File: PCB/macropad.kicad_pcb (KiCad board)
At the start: 2 copper layers, 80.5 x 100 mm, 46 parts, among them SW1 Kailh Choc V2, SW10 Kailh Choc V2, SW11 Kailh Choc V2, SW12 Kailh Choc V2, SW13 Kailh Choc V2, SW14 Kailh Choc V2, SW15 Kailh Choc V2, SW16 Kailh Choc V2, SW2 Kailh Choc V2, SW3 Kailh Choc V2, SW4 Kailh Choc V2, SW5 Kailh Choc V2, SW6 Kailh Choc V2, SW7 Kailh Choc V2, SW8 Kailh Choc V2, SW9 Kailh Choc V2, U2 SEEEDUINO XIAO RP2040

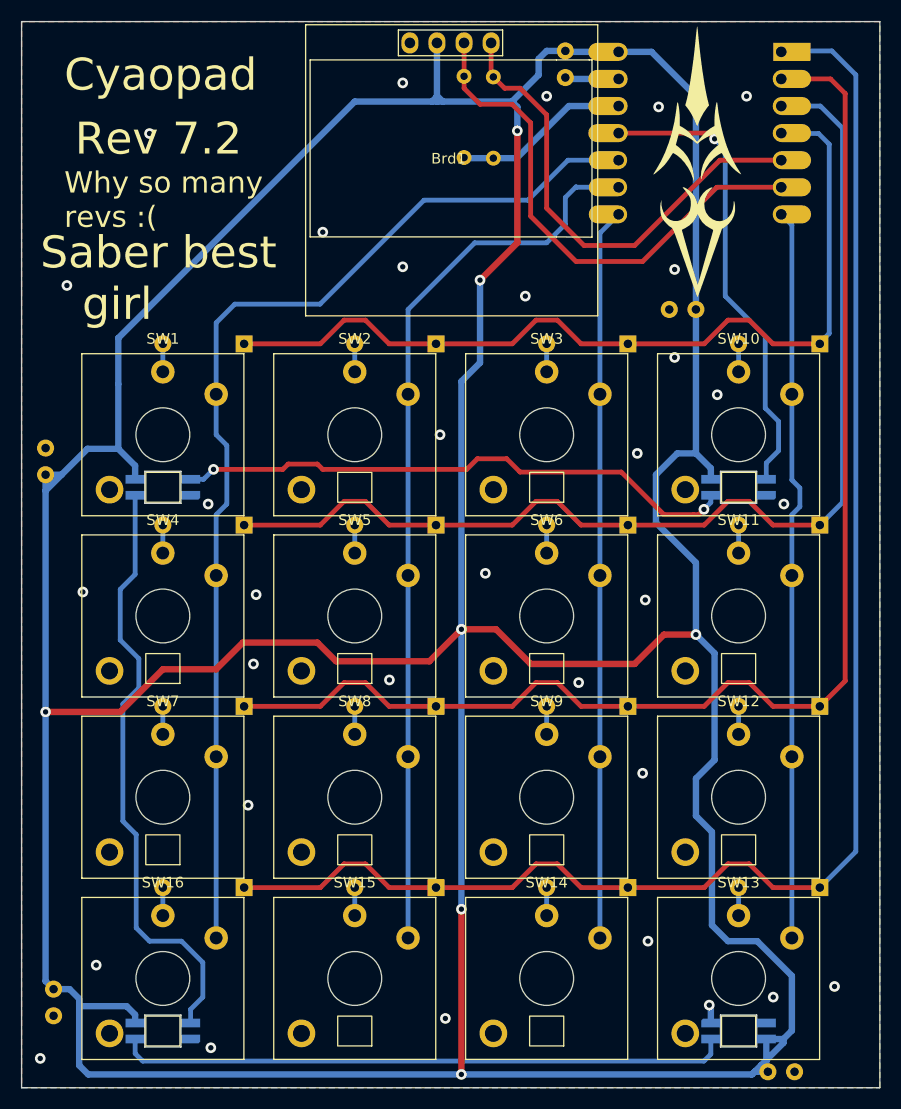
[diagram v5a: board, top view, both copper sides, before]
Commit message: Firmware path + clean up tracks
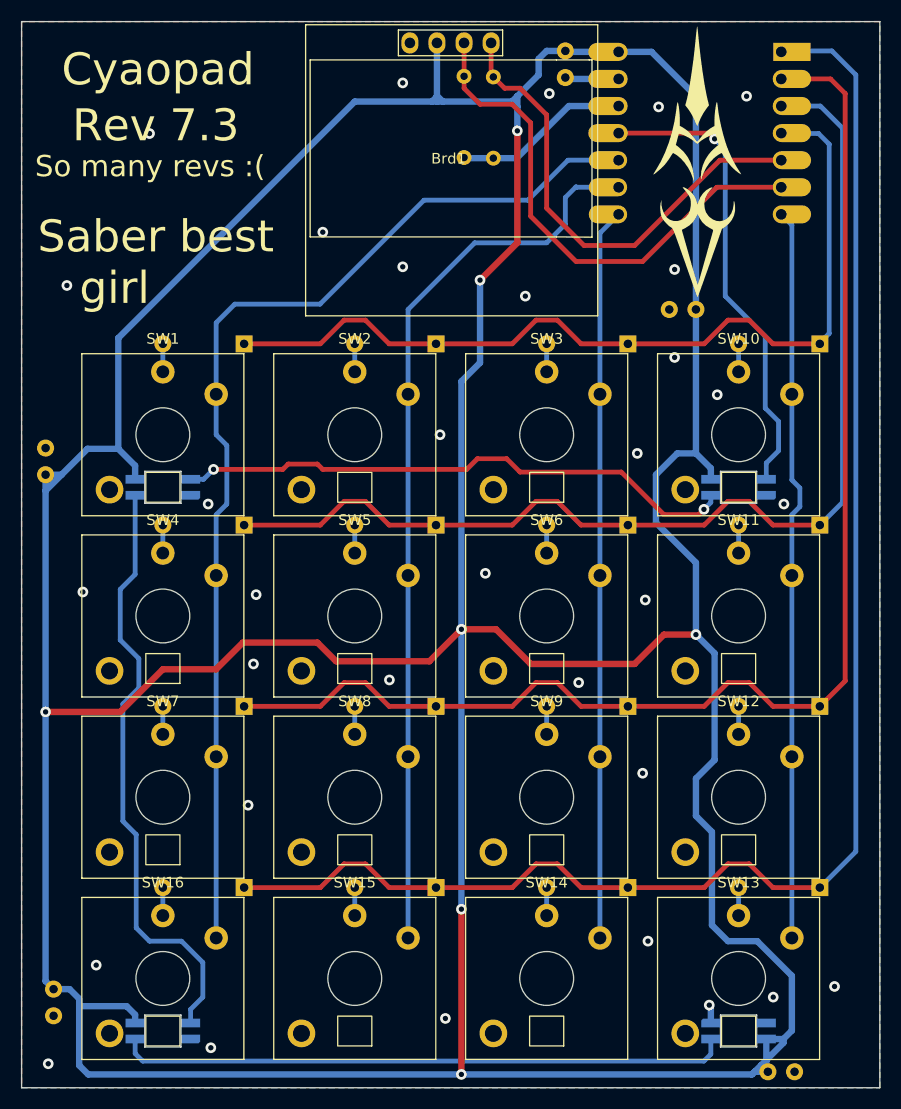
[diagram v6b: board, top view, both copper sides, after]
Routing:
- net +5V: track 502.4 -> 503.4 mm
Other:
- board text added: "Rev 7.3"
- board text added: "So many revs :("
- board text removed: "Rev 7.2"
- board text removed: "Why so many revs :("
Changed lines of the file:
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@@
     (title "Cyao macropad")
     (date "2024-09-23")
-    (rev "v7.2")
+    (rev "v7.3")
     (company "Cheyao")
     (comment 1 "https://github.com/cheyao/macropad")
@@
   (gr_line (start 185 150) (end 185 50)
     (stroke (width 0.05) (type default)) (layer "Edge.Cuts"))
-  (gr_text "Saber best\n   girl" (at 106.25 78.25) (layer "F.SilkS")
+  (gr_text "Saber best\n   girl" (at 106 76.75) (layer "F.SilkS")
     (effects (font (size 3 3) (thickness 0.3)) (justify left bottom))
   )
-  (gr_text "Rev 7.2" (at 109.5 62.75) (layer "F.SilkS")
+  (gr_text "Rev 7.3" (at 109.25 61.5) (layer "F.SilkS")
     (effects (font (size 3 3) (thickness 0.3)) (justify left bottom))
   )
-  (gr_text "Cyaopad" (at 108.5 56.75) (layer "F.SilkS")
+  (gr_text "Cyaopad" (at 108.25 56.25) (layer "F.SilkS")
     (effects (font (size 3 3) (thickness 0.3)) (justify left bottom))
   )
-  (gr_text "Why so many \nrevs :(" (at 108.5 69.5) (layer "F.SilkS")
+  (gr_text "So many revs :(" (at 105.75 64.75) (layer "F.SilkS")
     (effects (font (size 2 2) (thickness 0.3)) (justify left bottom))
   )
@@
   (via (at 165.75 73.25) (size 1) (drill 0.5) (layers "F.Cu" "B.Cu") (free) (net 26))
   (via (at 143.75 88.75) (size 1) (drill 0.5) (layers "F.Cu" "B.Cu") (free) (net 26))
-  (via (at 153.75 57) (size 1) (drill 0.5) (layers "F.Cu" "B.Cu") (free) (net 26))
+  (via (at 154 56.75) (size 1) (drill 0.5) (layers "F.Cu" "B.Cu") (free) (net 26))
   (via (at 148 101.75) (size 1) (drill 0.5) (layers "F.Cu" "B.Cu") (free) (net 26))
   (via (at 151.75 75.75) (size 1) (drill 0.5) (layers "F.Cu" "B.Cu") (free) (net 26))
-  (via (at 106.25 147.25) (size 1) (drill 0.5) (layers "F.Cu" "B.Cu") (free) (net 26))
+  (via (at 107 147.75) (size 1) (drill 0.5) (layers "F.Cu" "B.Cu") (free) (net 26))
   (via (at 126.25 110.25) (size 1) (drill 0.5) (layers "F.Cu" "B.Cu") (free) (net 26))
   (via (at 163 104.25) (size 1) (drill 0.5) (layers "F.Cu" "B.Cu") (free) (net 26))
@@
   (segment (start 143.46 52) (end 143.46 56.96) (width 0.6) (layer "B.Cu") (net 27))
   (segment (start 106.75 92.5) (end 108.25 92.5) (width 0.6) (layer "B.Cu") (net 27))
-  (segment (start 113.57 84) (end 113.57 90.07) (width 0.6) (layer "B.Cu") (net 27))
+  (segment (start 113.57 79.68) (end 113.57 90.07) (width 0.6) (layer "B.Cu") (net 27))
   (segment (start 173.875 147.875) (end 174.35 147.4) (width 0.6) (layer "B.Cu") (net 27))
   (segment (start 176.75 139.5) (end 176.75 144.64) (width 0.6) (layer "B.Cu") (net 27))
+  (segment (start 151 58) (end 151 57) (width 0.6) (layer "B.Cu") (net 27))
   (segment (start 113.57 79.68) (end 135.75 57.5) (width 0.6) (layer "B.Cu") (net 27))
   (segment (start 166 90.5) (end 164 92.5) (width 0.6) (layer "B.Cu") (net 27))
@@
   (segment (start 174.35 148.35) (end 174.5 148.5) (width 0.6) (layer "B.Cu") (net 27))
   (segment (start 175.96 145.43) (end 175.96 145.79) (width 0.6) (layer "B.Cu") (net 27))
+  (segment (start 151 57) (end 153 55) (width 0.6) (layer "B.Cu") (net 27))
   (segment (start 169.25 126) (end 169.25 134.75) (width 0.6) (layer "B.Cu") (net 27))
   (segment (start 110.75 148.75) (end 173 148.75) (width 0.6) (layer "B.Cu") (net 27))
@@
   (segment (start 114.35 142.35) (end 115.15 143.15) (width 0.6) (layer "B.Cu") (net 27))
   (segment (start 143.46 57.04) (end 143.5 57.08) (width 0.6) (layer "B.Cu") (net 27))
-  (segment (start 113.57 84) (end 113.57 79.68) (width 0.6) (layer "B.Cu") (net 27))
   (segment (start 144 57.5) (end 143.5 57.5) (width 0.6) (layer "B.Cu") (net 27))
+  (segment (start 150.5 57.5) (end 151 57) (width 0.6) (layer "B.Cu") (net 27))
   (segment (start 160.5 52.84) (end 155.59 52.84) (width 0.6) (layer "B.Cu") (net 27))
-  (segment (start 150.5 57.5) (end 153 55) (width 0.6) (layer "B.Cu") (net 27))
   (segment (start 106.75 92.5) (end 106.75 94) (width 0.6) (layer "B.Cu") (net 27))
   (segment (start 155.5 52.75) (end 155.59 52.84) (width 0.6) (layer "B.Cu") (net 27))
@@
   (segment (start 170.5 62) (end 169.5 61) (width 0.45) (layer "B.Cu") (net 30))
   (segment (start 170.5 75.75) (end 170.5 62) (width 0.45) (layer "B.Cu") (net 30))
-  (segment (start 160.75 92.25) (end 164.5 96) (width 0.45) (layer "F.Cu") (net 31))
-  (segment (start 164.75 96.25) (end 167.5 96.25) (width 0.45) (layer "F.Cu") (net 31))
+  (segment (start 160.75 92.25) (end 164.75 96.25) (width 0.45) (layer "F.Cu") (net 31))
+  (segment (start 164.75 96.25) (end 168 96.25) (width 0.45) (layer "F.Cu") (net 31))
   (segment (start 132.25 91.5) (end 132.75 92) (width 0.45) (layer "F.Cu") (net 31))
-  (segment (start 167.5 96.25) (end 168 96.25) (width 0.45) (layer "F.Cu") (net 31))
   (segment (start 129.5 91.5) (end 132.25 91.5) (width 0.45) (layer "F.Cu") (net 31))
   (segment (start 150 91) (end 151.25 92.25) (width 0.45) (layer "F.Cu") (net 31))
@@
   (segment (start 132.75 92) (end 146.25 92) (width 0.45) (layer "F.Cu") (net 31))
   (segment (start 122.5 92) (end 129 92) (width 0.45) (layer "F.Cu") (net 31))
-  (segment (start 164.5 96) (end 164.75 96.25) (width 0.45) (layer "F.Cu") (net 31))
   (segment (start 151.25 92.25) (end 160.75 92.25) (width 0.45) (layer "F.Cu") (net 31))
   (segment (start 146.25 92) (end 147.25 91) (width 0.45) (layer "F.Cu") (net 31))

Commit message: Change capacitor values and positions
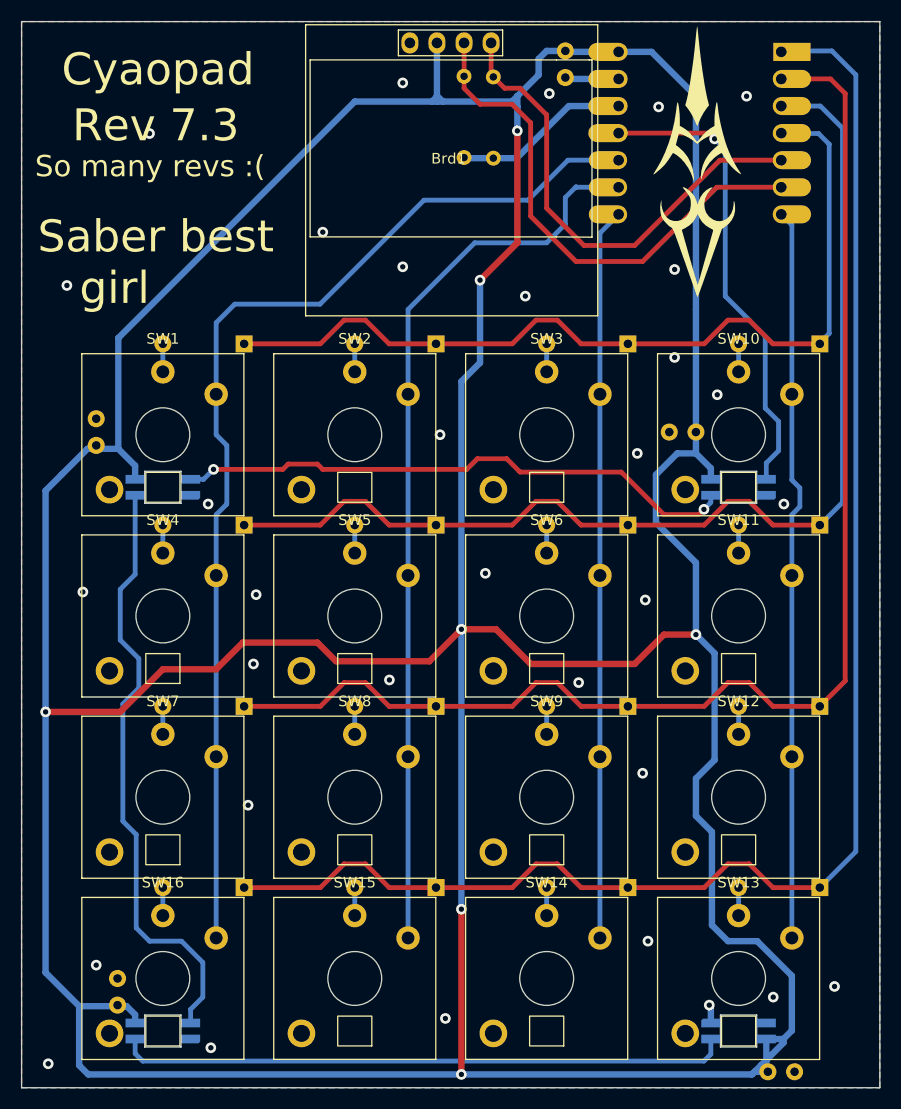
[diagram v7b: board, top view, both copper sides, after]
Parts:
- C1, C3, C4, C5: value 10pF -> 0.1uF
- moved C4 11.5 mm to (167.8, 88.5)
- moved C3 6.18 mm to (113.5, 142.2), turned to 90 degrees
- moved C5 5.49 mm to (111.5, 89.8)
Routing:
- net +5V: track 503.4 -> 499.5 mm

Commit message: Follow best practices and use stiching vias
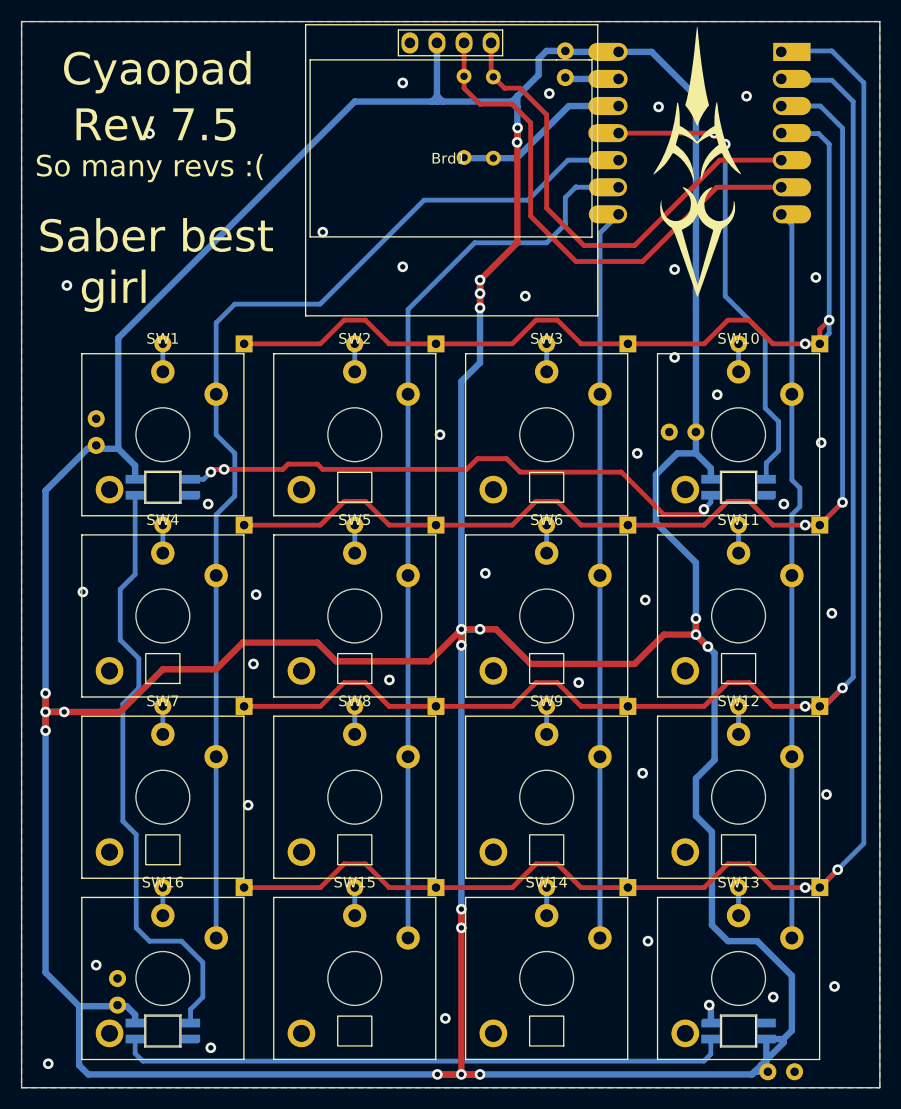
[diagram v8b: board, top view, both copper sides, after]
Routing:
- net +5V: track 499.5 -> 520.8 mm, vias 7 -> 20
- net ROW2: track 124.6 -> 129.6 mm, vias 0 -> 2
- net ROW1: track 104.2 -> 108.6 mm, vias 0 -> 2
- net ROW3: track 145.1 -> 149.5 mm, vias 0 -> 2
- net ROW0: track 83.6 -> 87.5 mm, vias 0 -> 2
- net LED: track 44.1 -> 45.9 mm, vias 1 -> 2
- net Net-(D17-DOUT): track 53.3 -> 54.7 mm, vias 2 -> 3
- net COL0: track 102.6 -> 103.2 mm
- net GND: vias 33 -> 37
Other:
- board text added: "Rev 7.5"
- board text removed: "Rev 7.3"
